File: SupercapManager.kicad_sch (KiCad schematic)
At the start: 10 parts, among them J1 JST4_F, J2 XT30_F, J3 XT30_F, J4 XT30_F, J5 XT30_F, J6 XT30_F, Q1 BSC059N04LS6, Q2 BSC059N04LS6

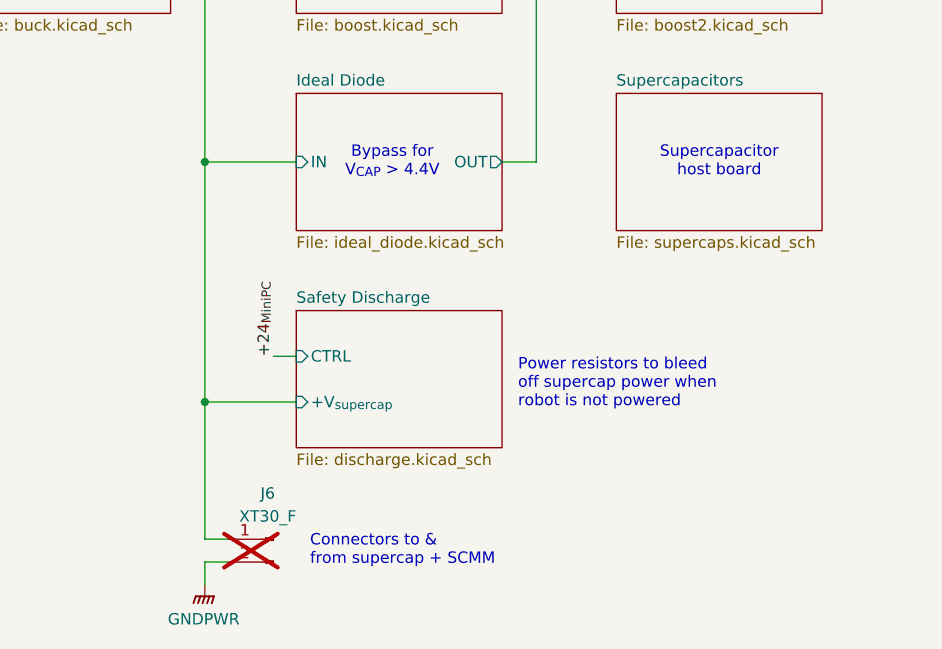
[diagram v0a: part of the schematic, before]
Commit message: Created seperate boards for supercap
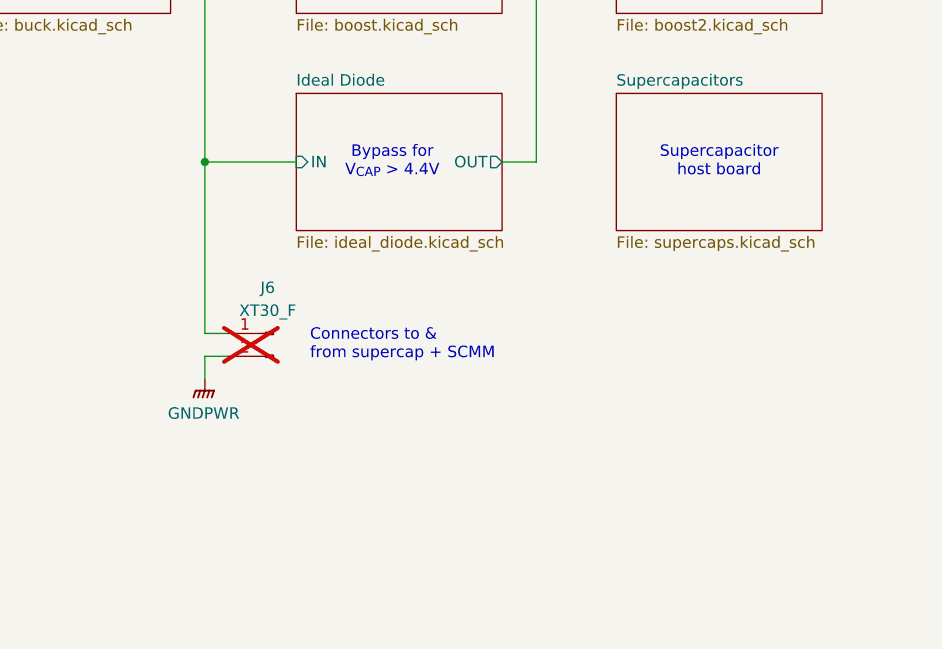
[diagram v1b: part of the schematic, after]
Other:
- removed sheet Safety Discharge
- note removed: "Power resistors to bleed off supercap power when robot is not powered"
- moved on the sheet: J6
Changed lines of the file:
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@@
 		)
 	)
-	(text "Power resistors to bleed\noff supercap power when\nrobot is not powered"
-		(exclude_from_sim no)
-		(at 160.528 154.178 0)
-		(effects
-			(font
-				(size 1.27 1.27)
-			)
-			(justify left)
-		)
-	)
 	(text "Senses & limits current\nout of the battery\nEnables supercapacitor charging"
 		(exclude_from_sim no)
@@
 	(text "Connectors to &\nfrom supercap + SCMM"
 		(exclude_from_sim no)
-		(at 137.414 172.72 0)
+		(at 137.414 149.86 0)
 		(effects
 			(font
@@
 	)
 	(junction
-		(at 125.73 156.21)
-		(diameter 0)
-		(color 0 0 0 0)
-	)
-	(junction
 		(at 198.12 96.52)
 		(diameter 0)
@@
 	(wire
 		(pts
-			(xy 125.73 156.21) (xy 125.73 171.45)
+			(xy 125.73 129.54) (xy 125.73 148.59)
 		)
 		(stroke
@@
 	(wire
 		(pts
-			(xy 128.27 173.99) (xy 125.73 173.99)
+			(xy 128.27 151.13) (xy 125.73 151.13)
 		)
 		(stroke
@@
 	(wire
 		(pts
-			(xy 133.35 151.13) (xy 135.89 151.13)
-		)
-		(stroke
-			(width 0)
-			(type default)
-		)
-	)
-	(wire
-		(pts
 			(xy 95.25 80.01) (xy 109.22 80.01)
 		)
@@
 	(wire
 		(pts
-			(xy 125.73 129.54) (xy 125.73 156.21)
-		)
-		(stroke
-			(width 0)
-			(type default)
-		)
-	)
-	(wire
-		(pts
-			(xy 125.73 173.99) (xy 125.73 176.53)
+			(xy 125.73 151.13) (xy 125.73 153.67)
 		)
 		(stroke
@@
 	(wire
 		(pts
-			(xy 128.27 171.45) (xy 125.73 171.45)
+			(xy 128.27 148.59) (xy 125.73 148.59)
 		)
 		(stroke
@@
 	(wire
 		(pts
-			(xy 125.73 156.21) (xy 135.89 156.21)
-		)
-		(stroke
-			(width 0)
-			(type default)
-		)
-	)
-	(wire
-		(pts
 			(xy 198.12 83.82) (xy 198.12 80.01)
 		)
@@
 	)
 	(label "+24_{MiniPC}"
-		(at 133.35 151.13 90)
-		(effects
-			(font
-				(size 1.27 1.27)
-			)
-			(justify left bottom)
-		)
-	)
-	(label "+24_{MiniPC}"
 		(at 123.19 40.64 0)
 		(effects
@@
 	(symbol
 		(lib_id "Connector:Conn_01x02_Pin")
-		(at 133.35 171.45 0)
+		(at 133.35 148.59 0)
 		(mirror y)
 		(unit 1)
@@
 		(dnp yes)
 		(property "Reference" "J6"
-			(at 132.715 166.37 0)
+			(at 132.715 143.51 0)
 			(effects
 				(font
@@
 		)
 		(property "Value" "XT30_F"
-			(at 132.715 168.91 0)
+			(at 132.715 146.05 0)
 			(effects
 				(font
@@
 		)
 		(property "Footprint" "Connector_AMASS:AMASS_XT30U-F_1x02_P5.0mm_Vertical"
-			(at 133.35 171.45 0)
+			(at 133.35 148.59 0)
 			(effects
 				(font
@@
 		)
 		(property "Datasheet" "~"
-			(at 133.35 171.45 0)
+			(at 133.35 148.59 0)
 			(effects
 				(font
@@
 		)
 		(property "Description" "Generic connector, single row, 01x02, script generated"
-			(at 133.35 171.45 0)
+			(at 133.35 148.59 0)
 			(effects
 				(font
@@
 		)
 		(property "Sim.Device" ""
-			(at 133.35 171.45 0)
+			(at 133.35 148.59 0)
 			(effects
 				(font
@@
 		)
 		(property "Sim.Pins" ""
-			(at 133.35 171.45 0)
+			(at 133.35 148.59 0)
 			(effects
 				(font
@@
 		)
 		(property "Sim.Type" ""
-			(at 133.35 171.45 0)
+			(at 133.35 148.59 0)
 			(effects
 				(font
@@
 		)
 		(property "Height" ""
-			(at 133.35 171.45 0)
+			(at 133.35 148.59 0)
 			(effects
 				(font
@@
 		)
 		(property "Manufacturer_Name" ""
-			(at 133.35 171.45 0)
+			(at 133.35 148.59 0)
 			(effects
 				(font
@@
 		)
 		(property "Manufacturer_Part_Number" ""
-			(at 133.35 171.45 0)
+			(at 133.35 148.59 0)
 			(effects
 				(font
@@
 		)
 		(property "Mouser Price/Stock" ""
-			(at 133.35 171.45 0)
+			(at 133.35 148.59 0)
 			(effects
 				(font
@@
 	(symbol
 		(lib_id "power:GNDPWR")
-		(at 125.73 176.53 0)
+		(at 125.73 153.67 0)
 		(unit 1)
 		(exclude_from_sim no)
@@
 		(fields_autoplaced yes)
 		(property "Reference" "#PWR015"
-			(at 125.73 181.61 0)
+			(at 125.73 158.75 0)
 			(effects
 				(font
@@
 		)
 		(property "Value" "GNDPWR"
-			(at 125.603 180.34 0)
+			(at 125.603 157.48 0)
 			(effects
 				(font
@@
 		)
 		(property "Footprint" ""
-			(at 125.73 177.8 0)
+			(at 125.73 154.94 0)
 			(effects
 				(font
@@
 		)
 		(property "Datasheet" ""
-			(at 125.73 177.8 0)
+			(at 125.73 154.94 0)
 			(effects
 				(font
@@
 		)
 		(property "Description" "Power symbol creates a global label with name \"GNDPWR\" , global ground"
-			(at 125.73 176.53 0)
+			(at 125.73 153.67 0)
 			(effects
 				(font
@@
 				)
 			)
-		)
-	)
-	(sheet
-		(at 135.89 146.05)
-		(size 22.86 15.24)
-		(exclude_from_sim no)
-		(in_bom yes)
-		(on_board yes)
-		(dnp no)
-		(fields_autoplaced yes)
-		(stroke
-			(width 0.1524)
-			(type solid)
-		)
-		(fill
-			(color 0 0 0 0.0000)
-		)
-		(property "Sheetname" "Safety Discharge"
-			(at 135.89 145.3384 0)
-			(effects
-				(font
-					(size 1.27 1.27)
-				)
-				(justify left bottom)
-			)
-		)
-		(property "Sheetfile" "discharge.kicad_sch"
-			(at 135.89 161.8746 0)
-			(effects
-				(font
-					(size 1.27 1.27)
-				)
-				(justify left top)
-			)
-		)
-		(pin "+V_{supercap}" input
-			(at 135.89 156.21 180)
-			(effects
-				(font
-					(size 1.27 1.27)
-				)
-				(justify left)
-			)
-		)
-		(pin "CTRL" input
-			(at 135.89 151.13 180)
-			(effects
-				(font
-					(size 1.27 1.27)
-				)
-				(justify left)
-			)
-		)
-		(instances
-			(project "SupercapManager"
-				(path "/6197145b-e7d4-44cc-9d90-537b6501bf60"
-					(page "4")
-				)
-			)

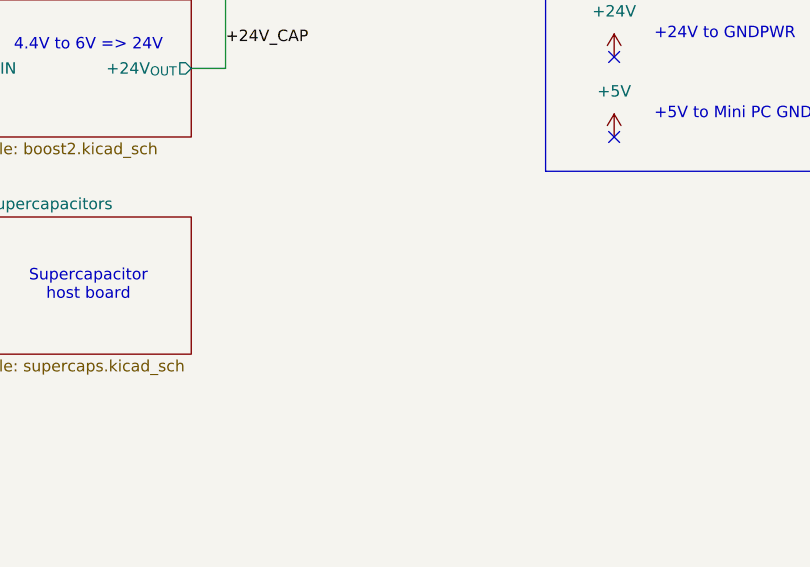
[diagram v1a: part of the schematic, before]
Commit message: Begin layout
Completed ideal diode layout
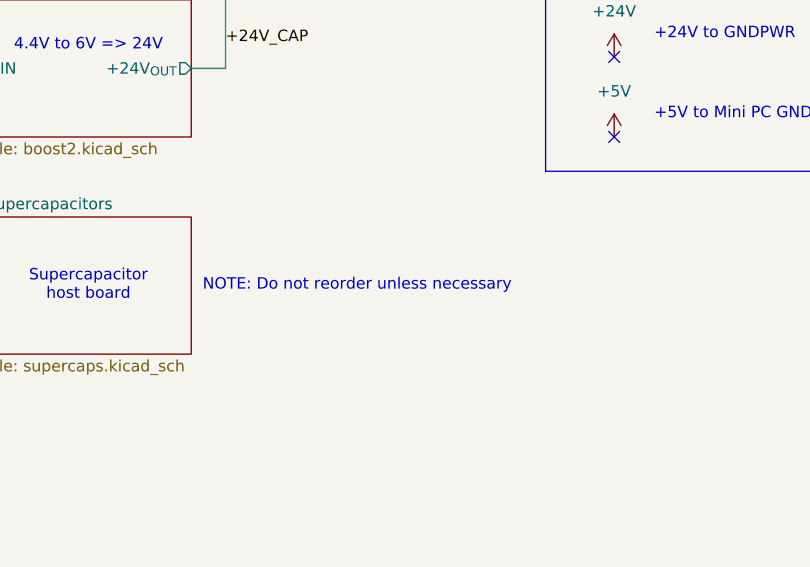
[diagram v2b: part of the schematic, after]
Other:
- note added: "NOTE: Do not reorder unless necessary"
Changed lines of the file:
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@@
 		)
 	)
+	(text "NOTE: Do not reorder unless necessary"
+		(exclude_from_sim no)
+		(at 195.58 129.54 0)
+		(effects
+			(font
+				(size 1.27 1.27)
+			)
+			(justify left)
+		)
+	)
 	(text "GND reference:"
 		(exclude_from_sim no)
@@
 		(size 22.86 15.24)
 		(exclude_from_sim no)
-		(in_bom yes)
-		(on_board yes)
+		(in_bom no)
+		(on_board no)
 		(dnp no)
 		(fields_autoplaced yes)
